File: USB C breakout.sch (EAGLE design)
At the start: 6 parts, among them J1 TYPE-C-31-M-12, X1 TSW-108-07-G-S

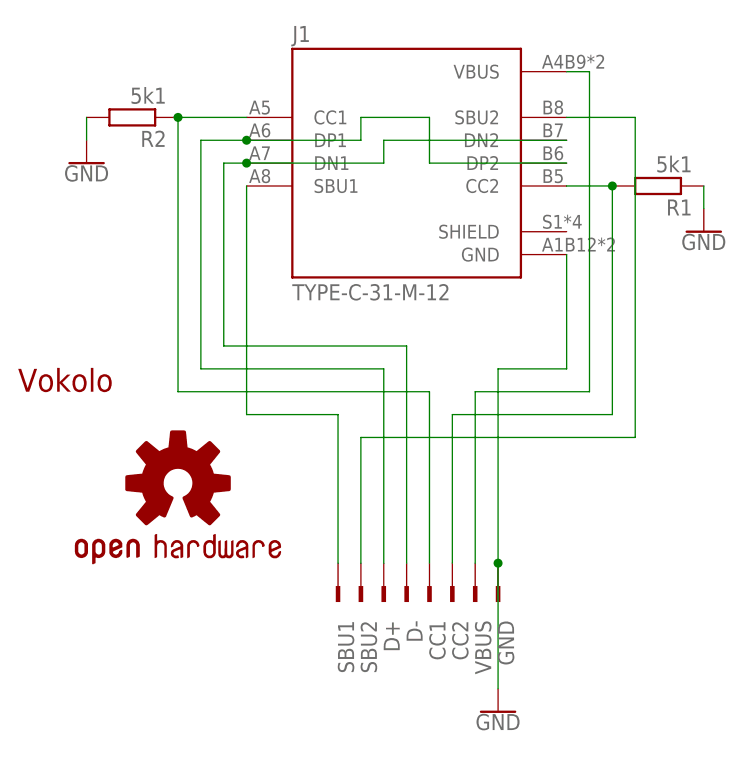
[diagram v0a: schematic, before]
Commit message: Add files via upload
New version USB-C breakout board.
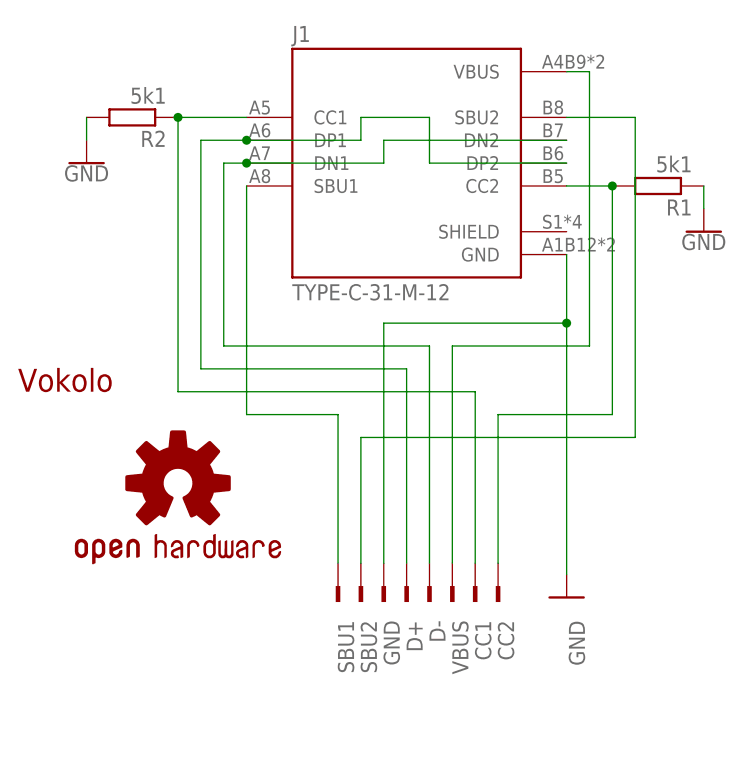
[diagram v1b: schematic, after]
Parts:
- LOGO1: value OSHW-LOGOMINI -> OSHW-LOGOS; device SparkFun-Aesthetics:OSHW-LOGOMINI -> SparkFun-Aesthetics:OSHW-LOGOS
- U$1: value LOGO_VOKOLO9,7MM -> LOGO_VOKOLO12MM; device logo_vokolo:LOGO_VOKOLO9,7MM -> logo_vokolo:LOGO_VOKOLO12MM
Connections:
- net CC1: now also X1-2.1; no longer X1-4.1
- net CC2: now also X1-1.1; no longer X1-3.1
- net D+: now also X1-5.1; no longer X1-6.1
- net D-: now also X1-4.1; no longer X1-5.1
- net GND: now also X1-6.1; no longer X1-1.1
- net VBUS: now also X1-3.1; no longer X1-2.1
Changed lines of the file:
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@@
 <part name="GND2" library="SparkFun-PowerSymbols" deviceset="GND" device=""/>
 <part name="GND3" library="SparkFun-PowerSymbols" deviceset="GND" device=""/>
-<part name="LOGO1" library="SparkFun-Aesthetics" deviceset="OSHW-LOGO" device="MINI"/>
-<part name="U$1" library="logo_vokolo" deviceset="LOGO_VOKOLO" device="9,7MM" value="LOGO_VOKOLO9,7MM"/>
+<part name="LOGO1" library="SparkFun-Aesthetics" deviceset="OSHW-LOGO" device="S" value="OSHW-LOGOS"/>
+<part name="U$1" library="logo_vokolo" deviceset="LOGO_VOKOLO" device="12MM" value="LOGO_VOKOLO12MM"/>
 </parts>
 <sheets>
@@
 <attribute name="VALUE" x="73.66" y="65.786" size="1.778" layer="96" align="top-center"/>
 </instance>
-<instance part="GND3" gate="1" x="50.8" y="12.7" smashed="yes">
-<attribute name="VALUE" x="50.8" y="12.446" size="1.778" layer="96" align="top-center"/>
+<instance part="GND3" gate="1" x="58.42" y="25.4" smashed="yes">
+<attribute name="VALUE" x="58.674" y="20.32" size="1.778" layer="96" rot="R90" align="top-center"/>
 </instance>
 <instance part="LOGO1" gate="G$1" x="15.24" y="38.1" smashed="yes"/>
@@
 <pinref part="J1" gate="G$1" pin="VBUS"/>
 <wire x1="58.42" y1="83.82" x2="60.96" y2="83.82" width="0.1524" layer="91"/>
-<wire x1="60.96" y1="83.82" x2="60.96" y2="48.26" width="0.1524" layer="91"/>
-<wire x1="60.96" y1="48.26" x2="48.26" y2="48.26" width="0.1524" layer="91"/>
-<pinref part="X1" gate="-2" pin="1"/>
-<wire x1="48.26" y1="29.21" x2="48.26" y2="48.26" width="0.1524" layer="91"/>
-<label x="48.26" y="22.86" size="1.778" layer="95" rot="R270"/>
+<wire x1="60.96" y1="83.82" x2="60.96" y2="53.34" width="0.1524" layer="91"/>
+<label x="45.72" y="22.86" size="1.778" layer="95" rot="R270"/>
+<wire x1="60.96" y1="53.34" x2="45.72" y2="53.34" width="0.1524" layer="91"/>
+<pinref part="X1" gate="-3" pin="1"/>
+<wire x1="45.72" y1="53.34" x2="45.72" y2="29.21" width="0.1524" layer="91"/>
 </segment>
 </net>
@@
 </segment>
 <segment>
+<pinref part="GND3" gate="1" pin="GND"/>
 <pinref part="J1" gate="G$1" pin="GND"/>
-<wire x1="58.42" y1="63.5" x2="58.42" y2="50.8" width="0.1524" layer="91"/>
-<wire x1="58.42" y1="50.8" x2="50.8" y2="50.8" width="0.1524" layer="91"/>
-<pinref part="X1" gate="-1" pin="1"/>
-<wire x1="50.8" y1="50.8" x2="50.8" y2="29.21" width="0.1524" layer="91"/>
-<label x="50.8" y="22.86" size="1.778" layer="95" rot="R270"/>
-<pinref part="GND3" gate="1" pin="GND"/>
-<wire x1="50.8" y1="15.24" x2="50.8" y2="29.21" width="0.1524" layer="91"/>
-<junction x="50.8" y="29.21"/>
+<wire x1="58.42" y1="63.5" x2="58.42" y2="55.88" width="0.1524" layer="91"/>
+<label x="38.1" y="22.86" size="1.778" layer="95" rot="R270"/>
+<pinref part="X1" gate="-6" pin="1"/>
+<wire x1="38.1" y1="29.21" x2="38.1" y2="55.88" width="0.1524" layer="91"/>
+<wire x1="38.1" y1="55.88" x2="58.42" y2="55.88" width="0.1524" layer="91"/>
+<wire x1="58.42" y1="27.94" x2="58.42" y2="55.88" width="0.1524" layer="91"/>
+<junction x="58.42" y="55.88"/>
 </segment>
 </net>
@@
 <wire x1="22.86" y1="73.66" x2="20.32" y2="73.66" width="0.1524" layer="91"/>
 <wire x1="20.32" y1="73.66" x2="20.32" y2="53.34" width="0.1524" layer="91"/>
-<wire x1="20.32" y1="53.34" x2="40.64" y2="53.34" width="0.1524" layer="91"/>
-<label x="40.64" y="22.86" size="1.778" layer="95" rot="R270"/>
+<wire x1="20.32" y1="53.34" x2="43.18" y2="53.34" width="0.1524" layer="91"/>
+<label x="43.18" y="22.86" size="1.778" layer="95" rot="R270"/>
 <wire x1="22.86" y1="73.66" x2="38.1" y2="73.66" width="0.1524" layer="91"/>
 <junction x="22.86" y="73.66"/>
@@
 <pinref part="J1" gate="G$1" pin="DN2"/>
 <wire x1="38.1" y1="76.2" x2="58.42" y2="76.2" width="0.1524" layer="91"/>
-<pinref part="X1" gate="-5" pin="1"/>
-<wire x1="40.64" y1="29.21" x2="40.64" y2="53.34" width="0.1524" layer="91"/>
+<pinref part="X1" gate="-4" pin="1"/>
+<wire x1="43.18" y1="53.34" x2="43.18" y2="29.21" width="0.1524" layer="91"/>
 </segment>
 </net>
@@
 <wire x1="22.86" y1="76.2" x2="17.78" y2="76.2" width="0.1524" layer="91"/>
 <wire x1="17.78" y1="76.2" x2="17.78" y2="50.8" width="0.1524" layer="91"/>
-<wire x1="17.78" y1="50.8" x2="38.1" y2="50.8" width="0.1524" layer="91"/>
-<label x="38.1" y="22.86" size="1.778" layer="95" rot="R270"/>
+<wire x1="17.78" y1="50.8" x2="40.64" y2="50.8" width="0.1524" layer="91"/>
+<label x="40.64" y="22.86" size="1.778" layer="95" rot="R270"/>
 <pinref part="J1" gate="G$1" pin="DP2"/>
 <wire x1="58.42" y1="73.66" x2="43.18" y2="73.66" width="0.1524" layer="91"/>
@@
 <wire x1="35.56" y1="76.2" x2="22.86" y2="76.2" width="0.1524" layer="91"/>
 <junction x="22.86" y="76.2"/>
-<pinref part="X1" gate="-6" pin="1"/>
-<wire x1="38.1" y1="29.21" x2="38.1" y2="50.8" width="0.1524" layer="91"/>
+<pinref part="X1" gate="-5" pin="1"/>
+<wire x1="40.64" y1="50.8" x2="40.64" y2="29.21" width="0.1524" layer="91"/>
 </segment>
 </net>
@@
 <wire x1="22.86" y1="78.74" x2="15.24" y2="78.74" width="0.1524" layer="91"/>
 <wire x1="15.24" y1="78.74" x2="15.24" y2="48.26" width="0.1524" layer="91"/>
-<label x="43.18" y="22.86" size="1.778" layer="95" rot="R270"/>
+<label x="48.26" y="22.86" size="1.778" layer="95" rot="R270"/>
 <pinref part="R2" gate="G$1" pin="1"/>
 <junction x="15.24" y="78.74"/>
-<wire x1="15.24" y1="48.26" x2="43.18" y2="48.26" width="0.1524" layer="91"/>
-<pinref part="X1" gate="-4" pin="1"/>
-<wire x1="43.18" y1="48.26" x2="43.18" y2="29.21" width="0.1524" layer="91"/>
+<wire x1="15.24" y1="48.26" x2="48.26" y2="48.26" width="0.1524" layer="91"/>
+<pinref part="X1" gate="-2" pin="1"/>
+<wire x1="48.26" y1="48.26" x2="48.26" y2="29.21" width="0.1524" layer="91"/>
 </segment>
 </net>
@@
 <pinref part="J1" gate="G$1" pin="CC2"/>
 <wire x1="63.5" y1="71.12" x2="58.42" y2="71.12" width="0.1524" layer="91"/>
-<label x="45.72" y="22.86" size="1.778" layer="95" rot="R270"/>
+<label x="50.8" y="22.86" size="1.778" layer="95" rot="R270"/>
 <pinref part="R1" gate="G$1" pin="2"/>
 <junction x="63.5" y="71.12"/>
-<wire x1="63.5" y1="45.72" x2="45.72" y2="45.72" width="0.1524" layer="91"/>
-<pinref part="X1" gate="-3" pin="1"/>
-<wire x1="45.72" y1="45.72" x2="45.72" y2="29.21" width="0.1524" layer="91"/>
+<wire x1="63.5" y1="45.72" x2="50.8" y2="45.72" width="0.1524" layer="91"/>
+<pinref part="X1" gate="-1" pin="1"/>
+<wire x1="50.8" y1="45.72" x2="50.8" y2="29.21" width="0.1524" layer="91"/>
 </segment>
 </net>
